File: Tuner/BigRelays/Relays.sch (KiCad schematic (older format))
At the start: 95 parts, among them J1 Conn_01x03, J10 Conn_01x02, J11 Conn_01x02, J12 Conn_01x01, J13 Conn_01x01, J14 Conn_01x01, J15 Conn_01x01, J16 Conn_01x02, J17 Conn_02x10_Odd_Even, J18 Conn_01x02, J19 Conn_01x03, J2 Conn_01x03, J21 Conn_01x01, J22 Conn_01x01, J23 Conn_01x01, J24 Conn_01x01, J25 Conn_01x01, J27 Conn_01x01, J28 Conn_01x01, J29 Conn_01x01, J3 Conn_01x03, J30 Conn_01x01, J4 Conn_01x03, J5 Conn_01x03, J6 Conn_01x03, J7 Conn_01x03, J8 Conn_01x02, J9 Conn_01x02

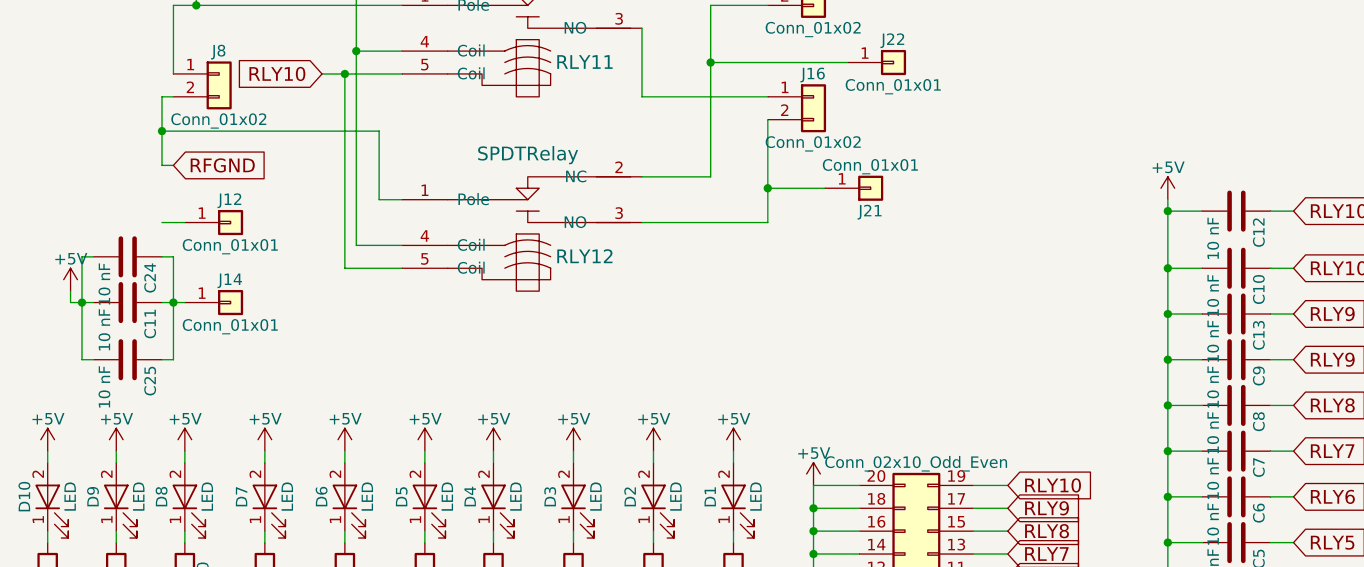
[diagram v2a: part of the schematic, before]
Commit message: Added extra capacitors to ground to large relay boards
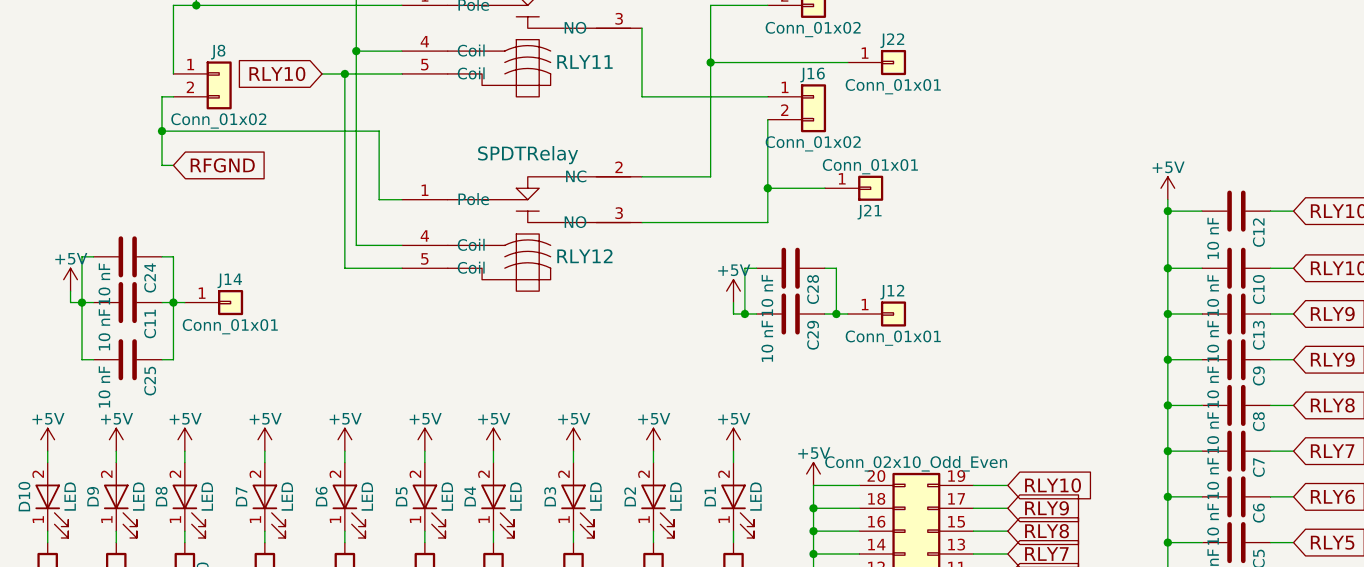
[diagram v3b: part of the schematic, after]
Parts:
- added C28, C29: 10 nF, Capacitors_THT:C_Disc_D5.0mm_W2.5mm_P5.00mm, symbol C
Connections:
- net +5V: now also C28.2, C29.2
- net at J12.1 (Pin_1): now also C28.1, C29.1
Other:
- moved on the sheet: J12
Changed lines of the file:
@@
 $EndComp
 $Comp
-L +5V #PWR10
+L +5V #PWR01
 U 1 1 5B1A3BAF
 P 2950 2950
-F 0 "#PWR10" H 2950 2800 50  0001 C CNN
+F 0 "#PWR01" H 2950 2800 50  0001 C CNN
 F 1 "+5V" H 2950 3090 50  0000 C CNN
 F 2 "" H 2950 2950 50  0001 C CNN
@@
 $EndComp
 $Comp
-L +5V #PWR16
+L +5V #PWR02
 U 1 1 5B1A3CC8
 P 4700 2950
-F 0 "#PWR16" H 4700 2800 50  0001 C CNN
+F 0 "#PWR02" H 4700 2800 50  0001 C CNN
 F 1 "+5V" H 4700 3090 50  0000 C CNN
 F 2 "" H 4700 2950 50  0001 C CNN
@@
 $EndComp
 $Comp
-L +5V #PWR19
+L +5V #PWR03
 U 1 1 5B1A3D42
 P 6450 2900
-F 0 "#PWR19" H 6450 2750 50  0001 C CNN
+F 0 "#PWR03" H 6450 2750 50  0001 C CNN
 F 1 "+5V" H 6450 3040 50  0000 C CNN
 F 2 "" H 6450 2900 50  0001 C CNN
@@
 $EndComp
 $Comp
-L +5V #PWR22
+L +5V #PWR04
 U 1 1 5B1A3DBC
 P 8100 4450
-F 0 "#PWR22" H 8100 4300 50  0001 C CNN
+F 0 "#PWR04" H 8100 4300 50  0001 C CNN
 F 1 "+5V" H 8100 4590 50  0000 C CNN
 F 2 "" H 8100 4450 50  0001 C CNN
@@
 $EndComp
 $Comp
-L +5V #PWR23
+L +5V #PWR05
 U 1 1 5B1A4C3F
 P 8250 1200
-F 0 "#PWR23" H 8250 1050 50  0001 C CNN
+F 0 "#PWR05" H 8250 1050 50  0001 C CNN
 F 1 "+5V" H 8250 1340 50  0000 C CNN
 F 2 "" H 8250 1200 50  0001 C CNN
@@
 $EndComp
 $Comp
-L +5V #PWR20
+L +5V #PWR06
 U 1 1 5B1A4CB9
 P 6500 1200
-F 0 "#PWR20" H 6500 1050 50  0001 C CNN
+F 0 "#PWR06" H 6500 1050 50  0001 C CNN
 F 1 "+5V" H 6500 1340 50  0000 C CNN
 F 2 "" H 6500 1200 50  0001 C CNN
@@
 $EndComp
 $Comp
-L +5V #PWR17
+L +5V #PWR07
 U 1 1 5B1A4D33
 P 4750 1150
-F 0 "#PWR17" H 4750 1000 50  0001 C CNN
+F 0 "#PWR07" H 4750 1000 50  0001 C CNN
 F 1 "+5V" H 4750 1290 50  0000 C CNN
 F 2 "" H 4750 1150 50  0001 C CNN
@@
 $EndComp
 $Comp
-L +5V #PWR11
+L +5V #PWR08
 U 1 1 5B1A4DAD
 P 3000 1150
-F 0 "#PWR11" H 3000 1000 50  0001 C CNN
+F 0 "#PWR08" H 3000 1000 50  0001 C CNN
 F 1 "+5V" H 3000 1290 50  0000 C CNN
 F 2 "" H 3000 1150 50  0001 C CNN
@@
 $EndComp
 $Comp
-L +5V #PWR4
+L +5V #PWR09
 U 1 1 5B25DE9C
 P 1450 6400
-F 0 "#PWR4" H 1450 6250 50  0001 C CNN
+F 0 "#PWR09" H 1450 6250 50  0001 C CNN
 F 1 "+5V" H 1450 6540 50  0000 C CNN
 F 2 "" H 1450 6400 50  0001 C CNN
@@
 $EndComp
 $Comp
-L +5V #PWR5
+L +5V #PWR010
 U 1 1 5B25F712
 P 1800 6400
-F 0 "#PWR5" H 1800 6250 50  0001 C CNN
+F 0 "#PWR010" H 1800 6250 50  0001 C CNN
 F 1 "+5V" H 1800 6540 50  0000 C CNN
 F 2 "" H 1800 6400 50  0001 C CNN
@@
 $EndComp
 $Comp
-L +5V #PWR6
+L +5V #PWR011
 U 1 1 5B25F91B
 P 2150 6400
-F 0 "#PWR6" H 2150 6250 50  0001 C CNN
+F 0 "#PWR011" H 2150 6250 50  0001 C CNN
 F 1 "+5V" H 2150 6540 50  0000 C CNN
 F 2 "" H 2150 6400 50  0001 C CNN
@@
 $EndComp
 $Comp
-L +5V #PWR8
+L +5V #PWR012
 U 1 1 5B25F931
 P 2500 6400
-F 0 "#PWR8" H 2500 6250 50  0001 C CNN
+F 0 "#PWR012" H 2500 6250 50  0001 C CNN
 F 1 "+5V" H 2500 6540 50  0000 C CNN
 F 2 "" H 2500 6400 50  0001 C CNN
@@
 $EndComp
 $Comp
-L +5V #PWR9
+L +5V #PWR013
 U 1 1 5B25FB4D
 P 2800 6400
-F 0 "#PWR9" H 2800 6250 50  0001 C CNN
+F 0 "#PWR013" H 2800 6250 50  0001 C CNN
 F 1 "+5V" H 2800 6540 50  0000 C CNN
 F 2 "" H 2800 6400 50  0001 C CNN
@@
 $EndComp
 $Comp
-L +5V #PWR12
+L +5V #PWR014
 U 1 1 5B25FB63
 P 3150 6400
-F 0 "#PWR12" H 3150 6250 50  0001 C CNN
+F 0 "#PWR014" H 3150 6250 50  0001 C CNN
 F 1 "+5V" H 3150 6540 50  0000 C CNN
 F 2 "" H 3150 6400 50  0001 C CNN
@@
 $EndComp
 $Comp
-L +5V #PWR13
+L +5V #PWR015
 U 1 1 5B25FB79
 P 3500 6400
-F 0 "#PWR13" H 3500 6250 50  0001 C CNN
+F 0 "#PWR015" H 3500 6250 50  0001 C CNN
 F 1 "+5V" H 3500 6540 50  0000 C CNN
 F 2 "" H 3500 6400 50  0001 C CNN
@@
 $EndComp
 $Comp
-L +5V #PWR14
+L +5V #PWR016
 U 1 1 5B25FB8F
 P 3850 6400
-F 0 "#PWR14" H 3850 6250 50  0001 C CNN
+F 0 "#PWR016" H 3850 6250 50  0001 C CNN
 F 1 "+5V" H 3850 6540 50  0000 C CNN
 F 2 "" H 3850 6400 50  0001 C CNN
@@
 RLY10
 $Comp
-L +5V #PWR15
+L +5V #PWR017
 U 1 1 5B89A678
 P 4200 6550
-F 0 "#PWR15" H 4200 6400 50  0001 C CNN
+F 0 "#PWR017" H 4200 6400 50  0001 C CNN
 F 1 "+5V" H 4200 6690 50  0000 C CNN
 F 2 "" H 4200 6550 50  0001 C CNN
@@
 $EndComp
 $Comp
-L +5V #PWR3
+L +5V #PWR018
 U 1 1 5B89BB19
 P 1150 6400
-F 0 "#PWR3" H 1150 6250 50  0001 C CNN
+F 0 "#PWR018" H 1150 6250 50  0001 C CNN
 F 1 "+5V" H 1150 6540 50  0000 C CNN
 F 2 "" H 1150 6400 50  0001 C CNN
@@
 $EndComp
 $Comp
-L +5V #PWR1
+L +5V #PWR019
 U 1 1 5B89BBCB
 P 850 6400
-F 0 "#PWR1" H 850 6250 50  0001 C CNN
+F 0 "#PWR019" H 850 6250 50  0001 C CNN
 F 1 "+5V" H 850 6540 50  0000 C CNN
 F 2 "" H 850 6400 50  0001 C CNN
@@
 RLY9
 $Comp
-L +5V #PWR18
+L +5V #PWR020
 U 1 1 5B89FB34
 P 5750 5300
-F 0 "#PWR18" H 5750 5150 50  0001 C CNN
+F 0 "#PWR020" H 5750 5150 50  0001 C CNN
 F 1 "+5V" H 5750 5440 50  0000 C CNN
 F 2 "" H 5750 5300 50  0001 C CNN
@@
 RLY8
 $Comp
-L +5V #PWR21
+L +5V #PWR021
 U 1 1 5B8A1B7B
 P 8100 2900
-F 0 "#PWR21" H 8100 2750 50  0001 C CNN
+F 0 "#PWR021" H 8100 2750 50  0001 C CNN
 F 1 "+5V" H 8100 3040 50  0000 C CNN
 F 2 "" H 8100 2900 50  0001 C CNN
@@
 $EndComp
 $Comp
-L +5V #PWR7
+L +5V #PWR022
 U 1 1 5B8A2542
 P 2200 4350
-F 0 "#PWR7" H 2200 4200 50  0001 C CNN
+F 0 "#PWR022" H 2200 4200 50  0001 C CNN
 F 1 "+5V" H 2200 4490 50  0000 C CNN
 F 2 "" H 2200 4350 50  0001 C CNN
@@
 $EndComp
 $Comp
-L +5V #PWR2
+L +5V #PWR023
 U 1 1 5B97C780
 P 950 5700
-F 0 "#PWR2" H 950 5550 50  0001 C CNN
+F 0 "#PWR023" H 950 5550 50  0001 C CNN
 F 1 "+5V" H 950 5840 50  0000 C CNN
 F 2 "" H 950 5700 50  0001 C CNN
@@
 RLY9
 $Comp
-L +5V #PWR25
+L +5V #PWR024
 U 1 1 5BA3849B
 P 10250 1300
-F 0 "#PWR25" H 10250 1150 50  0001 C CNN
+F 0 "#PWR024" H 10250 1150 50  0001 C CNN
 F 1 "+5V" H 10250 1440 50  0000 C CNN
 F 2 "" H 10250 1300 50  0001 C CNN
@@
 L Conn_01x01 J12
 U 1 1 5B1981D8
-P 1650 5400
-F 0 "J12" H 1650 5500 50  0000 C CNN
-F 1 "Conn_01x01" H 1650 5300 50  0000 C CNN
-F 2 "Connectors:1pin" H 1650 5400 50  0001 C CNN
-F 3 "" H 1650 5400 50  0001 C CNN
-	1    1650 5400
+P 4550 5800
+F 0 "J12" H 4550 5900 50  0000 C CNN
+F 1 "Conn_01x01" H 4550 5700 50  0000 C CNN
+F 2 "Connectors:1pin" H 4550 5800 50  0001 C CNN
+F 3 "" H 4550 5800 50  0001 C CNN
+	1    4550 5800
 	1    0    0    -1
 $EndComp
@@
 	1350 5550 1400 5550
 Wire Wire Line
-	1350 5400 1450 5400
-Wire Wire Line
 	7950 5400 8300 5400
 Wire Wire Line
@@
 Connection ~ 5750 5800
 Wire Wire Line
-	5900 5800 5750 5800
+	5750 5800 5900 5800
 Wire Wire Line
 	5750 5300 5750 7600
@@
 	2600 1400 3050 1400
 $Comp
-L +5V #PWR24
+L +5V #PWR025
 U 1 1 5DDB7F4F
 P 10150 3500
-F 0 "#PWR24" H 10150 3350 50  0001 C CNN
+F 0 "#PWR025" H 10150 3350 50  0001 C CNN
 F 1 "+5V" H 10150 3640 50  0000 C CNN
 F 2 "" H 10150 3500 50  0001 C CNN
@@
 	10700 3500 10750 3500
 $Comp
-L +5V #PWR26
+L +5V #PWR026
 U 1 1 5DDB884A
 P 10400 4750
-F 0 "#PWR26" H 10400 4600 50  0001 C CNN
+F 0 "#PWR026" H 10400 4600 50  0001 C CNN
 F 1 "+5V" H 10400 4890 50  0000 C CNN
 F 2 "" H 10400 4750 50  0001 C CNN
@@
 	10850 4400 10850 4750
 Connection ~ 10700 4400
+$Comp
+L C C29
+U 1 1 5DDC0377
+P 4100 5800
+F 0 "C29" H 4125 5900 50  0000 L CNN
+F 1 "10 nF" H 4125 5700 50  0000 L CNN
+F 2 "Capacitors_THT:C_Disc_D5.0mm_W2.5mm_P5.00mm" H 4138 5650 50  0001 C CNN
+F 3 "" H 4100 5800 50  0001 C CNN
+	1    4100 5800
+	0    1    1    0
+$EndComp
+$Comp
+L +5V #PWR027
+U 1 1 5DDC037D
+P 3850 5750
+F 0 "#PWR027" H 3850 5600 50  0001 C CNN
+F 1 "+5V" H 3850 5890 50  0000 C CNN
+F 2 "" H 3850 5750 50  0001 C CNN
+F 3 "" H 3850 5750 50  0001 C CNN
+	1    3850 5750
+	1    0    0    -1
+$EndComp
+$Comp
+L C C28
+U 1 1 5DDC0383
+P 4100 5600
+F 0 "C28" H 4125 5700 50  0000 L CNN
+F 1 "10 nF" H 4125 5500 50  0000 L CNN
+F 2 "Capacitors_THT:C_Disc_D5.0mm_W2.5mm_P5.00mm" H 4138 5450 50  0001 C CNN
+F 3 "" H 4100 5600 50  0001 C CNN
+	1    4100 5600
+	0    1    1    0
+$EndComp
+Connection ~ 3900 5800
+Wire Wire Line
+	3900 5600 3900 5800
+Connection ~ 4300 5800
+Wire Wire Line
+	4300 5600 4300 5800
+Wire Wire Line
+	4250 5800 4350 5800
+Wire Wire Line
+	3850 5800 3950 5800
+Wire Wire Line
+	3850 5750 3850 5800
+Wire Wire Line
+	4300 5600 4250 5600
+Wire Wire Line
+	3950 5600 3900 5600
 $EndSCHEMATC
